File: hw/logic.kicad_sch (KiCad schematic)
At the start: 26 parts, among them J2 UART, J3 JTAG, SW1 SW_Push, SW2 SW_Push, U1 ESP32-C6-MINI-1/U, Y1 32.768k

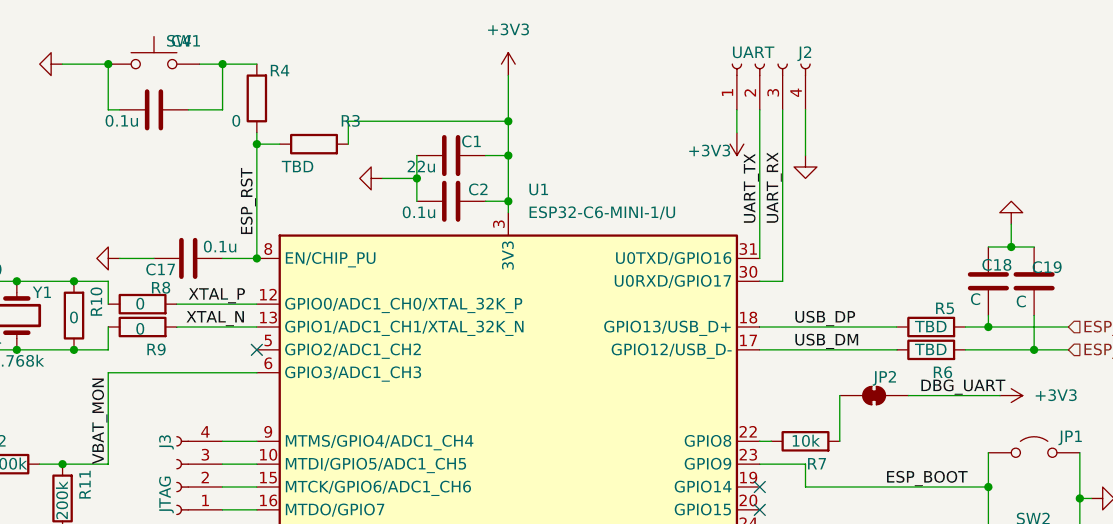
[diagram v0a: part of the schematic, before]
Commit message: Replace case, start on Power stages
I've replaced the case STL with one that's better in every way, it prints faster, doesn't need supports, and the holder for the diffuser is better,

I may still tweak the design but I'm happy with it for now.
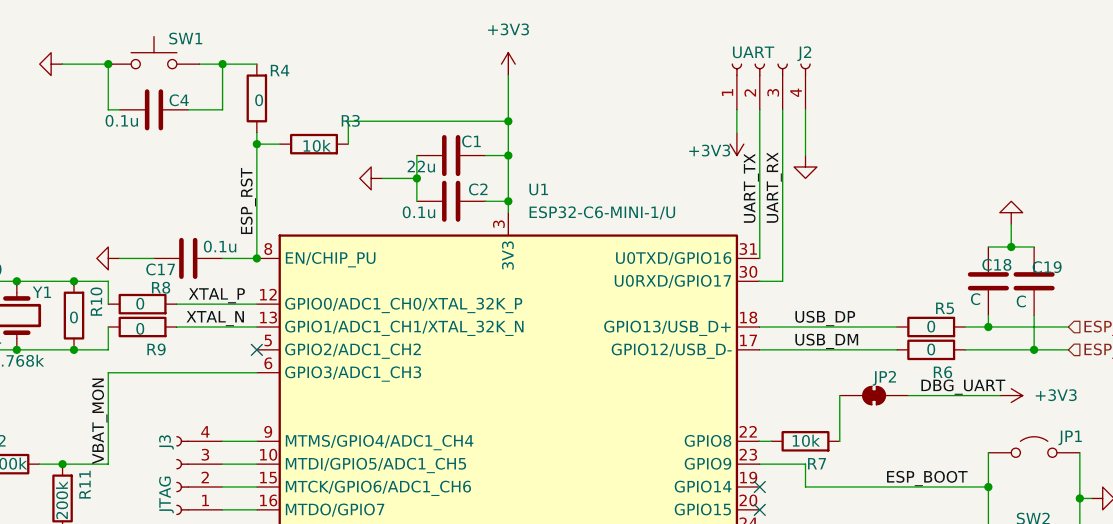
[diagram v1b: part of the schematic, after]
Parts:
- R3: value TBD -> 10k
- R5, R6: value TBD -> 0
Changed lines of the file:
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@@
 		(dnp no)
 		(property "Reference" "C4"
-			(at 97.028 43.18 90)
+			(at 96.774 49.784 90)
 			(effects
 				(font
@@
 			)
 		)
-		(property "Value" "TBD"
+		(property "Value" "0"
 			(at 180.34 74.93 90)
 			(effects
@@
 		(dnp no)
 		(property "Reference" "SW1"
-			(at 97.282 43.18 0)
+			(at 97.536 42.926 0)
 			(effects
 				(font
@@
 			)
 		)
-		(property "Value" "TBD"
-			(at 109.982 57.15 90)
+		(property "Value" "10k"
+			(at 112.014 54.864 90)
 			(effects
 				(font
@@
 		)
 		(property "Value" "0"
-			(at 103.124 52.07 0)
+			(at 105.664 49.784 0)
 			(effects
 				(font
@@
 			)
 		)
-		(property "Value" "TBD"
+		(property "Value" "0"
 			(at 180.34 77.47 90)
 			(effects

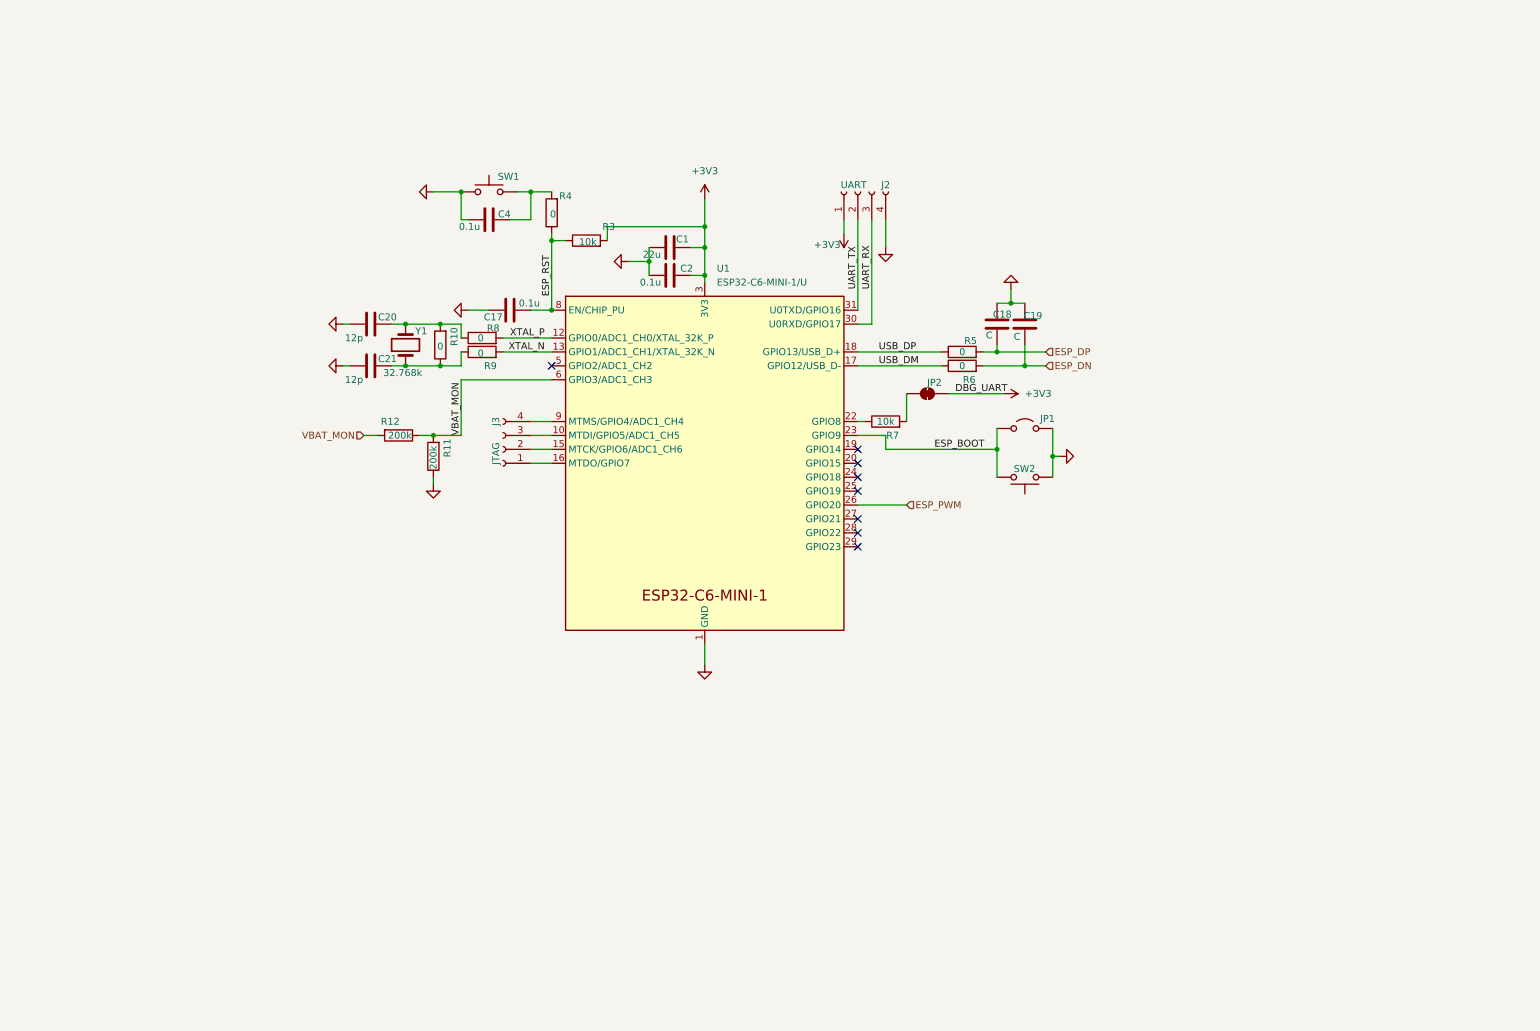
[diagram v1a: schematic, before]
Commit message: Finish power stage, work on other stages
Power stage should be finalised, I've updated LED stage to include a solder jumper, to allow up to half of the LEDs to be removed in the case of power/cost savings
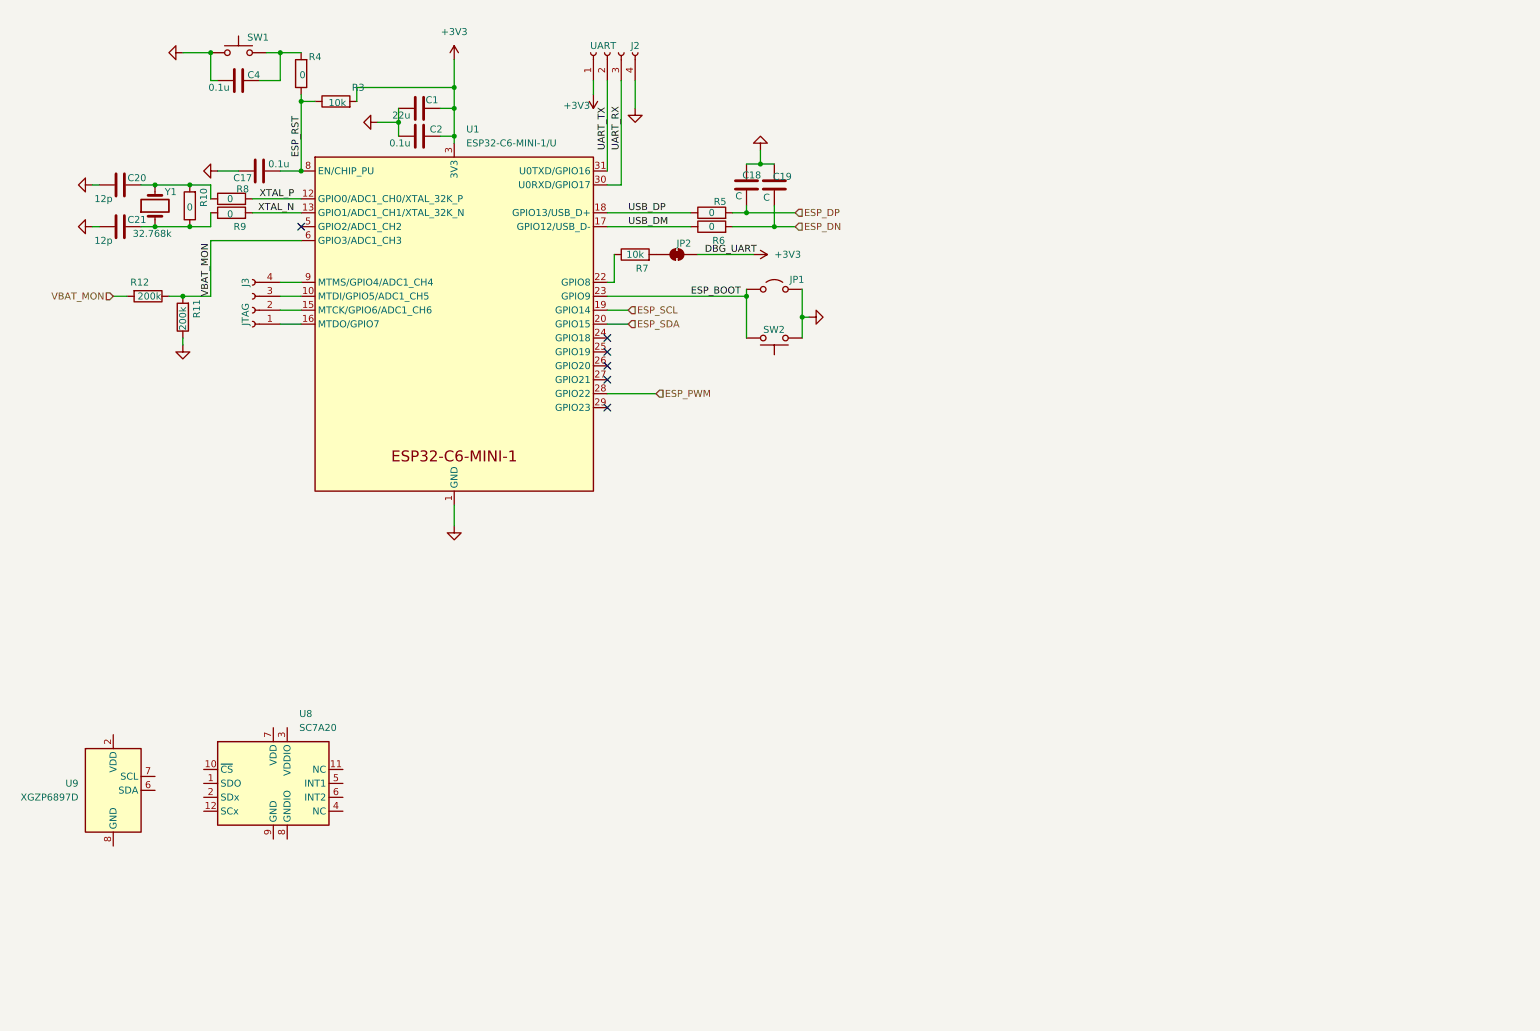
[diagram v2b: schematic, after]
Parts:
- added U8: SC7A20, Package_LGA:LGA-12_2x2mm_P0.5mm, symbol Sensor_Motion:SC7A20
- added U9: XGZP6897D, Sensor_Pressure:CFSensor_XGZP6897x, symbol Sensor_Pressure:XGZP6897D
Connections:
- net ESP_PWM: now also U1.28 (GPIO22); no longer U1.26 (GPIO20)
- net ESP_SCL: now reaches U1.19 (GPIO14)
- net ESP_SDA: now reaches U1.20 (GPIO15)
- no-connect marks 8 -> 6
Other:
- moved on the sheet: C1, C17, C18, C19, C2, C20, C21, C4, J2, J3, JP1, JP2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

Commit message: Work on footprinting and PCB
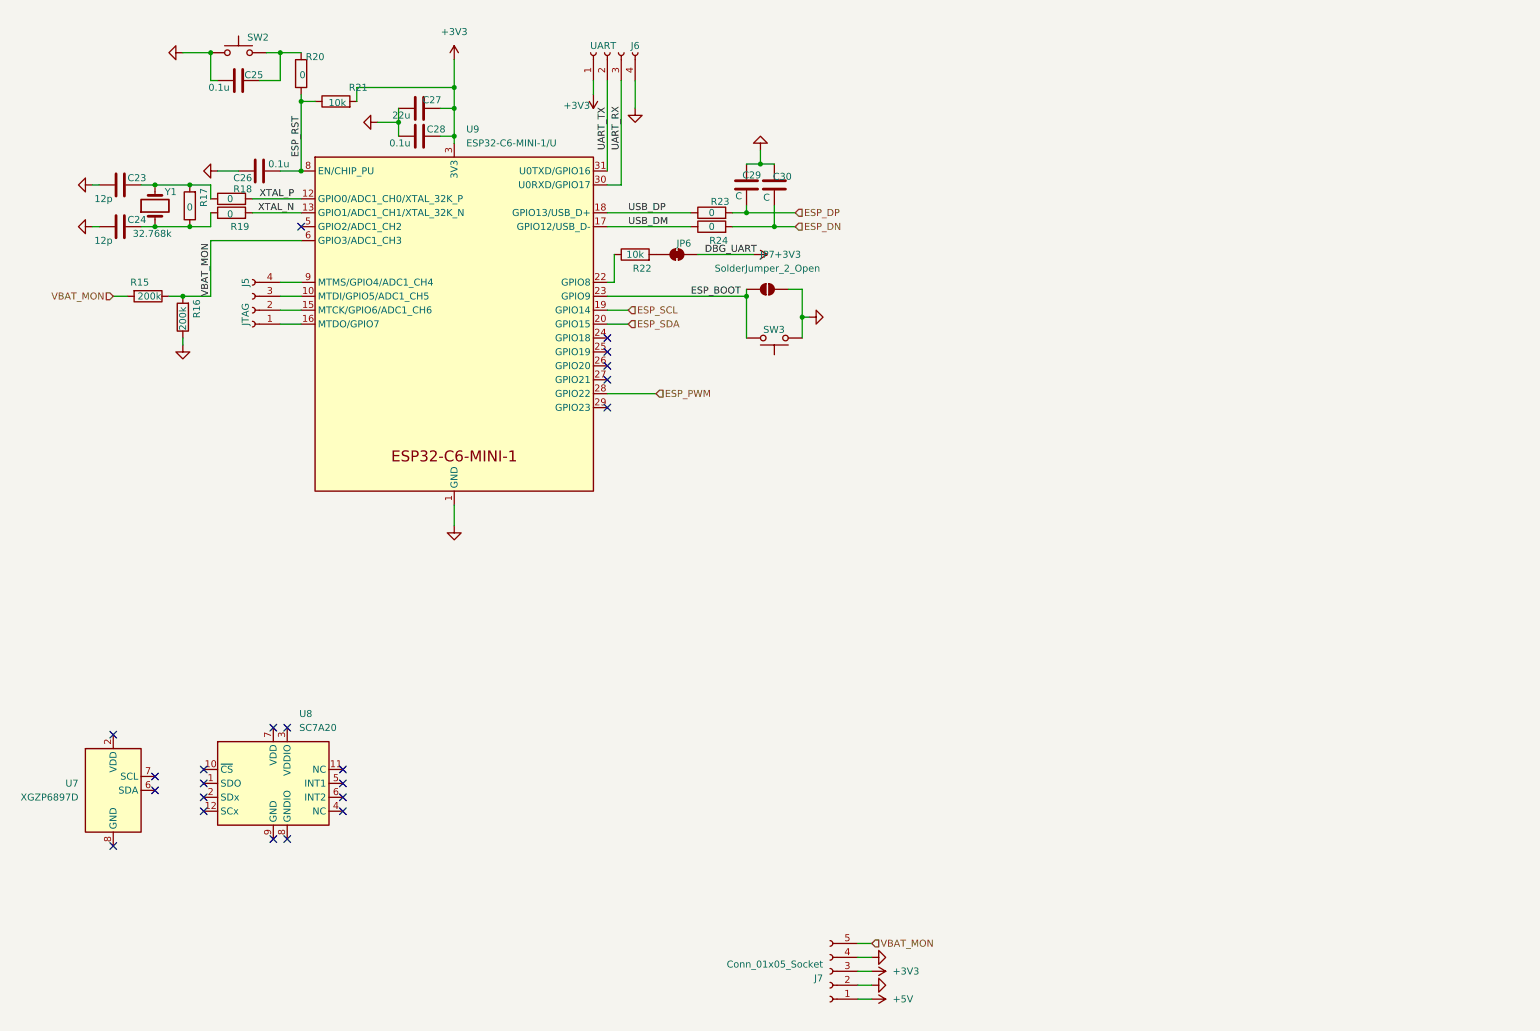
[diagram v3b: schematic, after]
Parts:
- removed JP1: Jumper_2_Open, symbol Jumper:Jumper_2_Open
- added J7: Conn_01x05_Socket, Connector_JST:JST_EH_B5B-EH-A_1x05_P2.50mm_Vertical, symbol Connector:Conn_01x05_Socket
- added JP7: SolderJumper_2_Open, Jumper:SolderJumper-2_P1.3mm_Open_TrianglePad1.0x1.5mm, symbol Jumper:SolderJumper_2_Open
- C23: renamed from C20; footprint (none) -> Capacitor_SMD:C_0603_1608Metric
- C24: renamed from C21; footprint (none) -> Capacitor_SMD:C_0603_1608Metric
- C25: renamed from C4; footprint (none) -> Capacitor_SMD:C_0603_1608Metric
- C26: renamed from C17; footprint (none) -> Capacitor_SMD:C_0603_1608Metric
- C27: renamed from C1; footprint (none) -> Capacitor_SMD:C_1206_3216Metric
- C28: renamed from C2; footprint (none) -> Capacitor_SMD:C_0603_1608Metric
- J5: renamed from J3; footprint (none) -> Connector_JST:JST_EH_B4B-EH-A_1x04_P2.50mm_Vertical
- J6: renamed from J2; footprint (none) -> Connector_JST:JST_XH_B4B-XH-A_1x04_P2.50mm_Vertical
- JP6: renamed from JP2; footprint (none) -> Jumper:SolderJumper-2_P1.3mm_Bridged_Pad1.0x1.5mm
- R17: renamed from R10; footprint (none) -> PCM_Resistor_SMD_AKL:R_0805_2012Metric
- R18: renamed from R8; footprint (none) -> PCM_Resistor_SMD_AKL:R_0805_2012Metric
- R19: renamed from R9; footprint (none) -> PCM_Resistor_SMD_AKL:R_0805_2012Metric
- R20: renamed from R4; footprint (none) -> PCM_Resistor_SMD_AKL:R_0805_2012Metric
- R23: renamed from R5; footprint (none) -> PCM_Resistor_SMD_AKL:R_0805_2012Metric
- R24: renamed from R6; footprint (none) -> PCM_Resistor_SMD_AKL:R_0805_2012Metric
- SW2: renamed from SW1; footprint (none) -> Button_Switch_THT:SW_Tactile_SPST_Angled_PTS645Vx31-2LFS
- SW3: renamed from SW2; footprint (none) -> Button_Switch_THT:SW_Tactile_SPST_Angled_PTS645Vx31-2LFS
- Y1: footprint (none) -> Crystal:Crystal_C26-LF_D2.1mm_L6.5mm_Horizontal
- renumbered C18 to C29, C19 to C30, R12 to R15, R11 to R16, R3 to R21, R7 to R22, U9 to U7, U1 to U9
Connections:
- net +3V3: now also J7.3 (Pin_3)
- net ESP_BOOT: now also JP7.1 (A)
- net GND: now also J7.2 (Pin_2), J7.4 (Pin_4), JP7.2 (B)
- net VBAT_MON: now also J7.5 (Pin_5)
- new net +5V: J7.1 (Pin_1)
- no-connect marks 6 -> 22
